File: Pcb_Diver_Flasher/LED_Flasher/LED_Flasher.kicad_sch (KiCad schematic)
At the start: 24 parts, among them IC100 PIC16LF15313, IC101 MP3217, J100 SKEDD6, SW100 MK15-C2, T100 MJD122T4

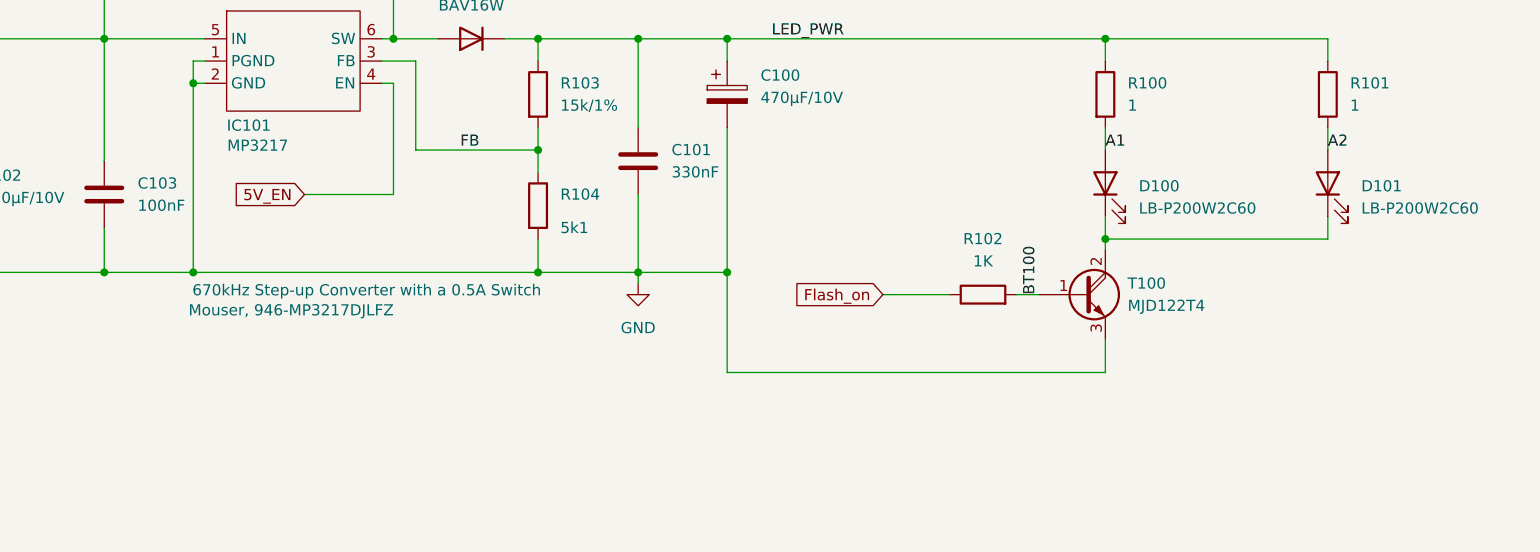
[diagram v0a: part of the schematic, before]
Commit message: New datasheets and simulations added. Target is to improve the power of the booster circuit of the diver flasher.
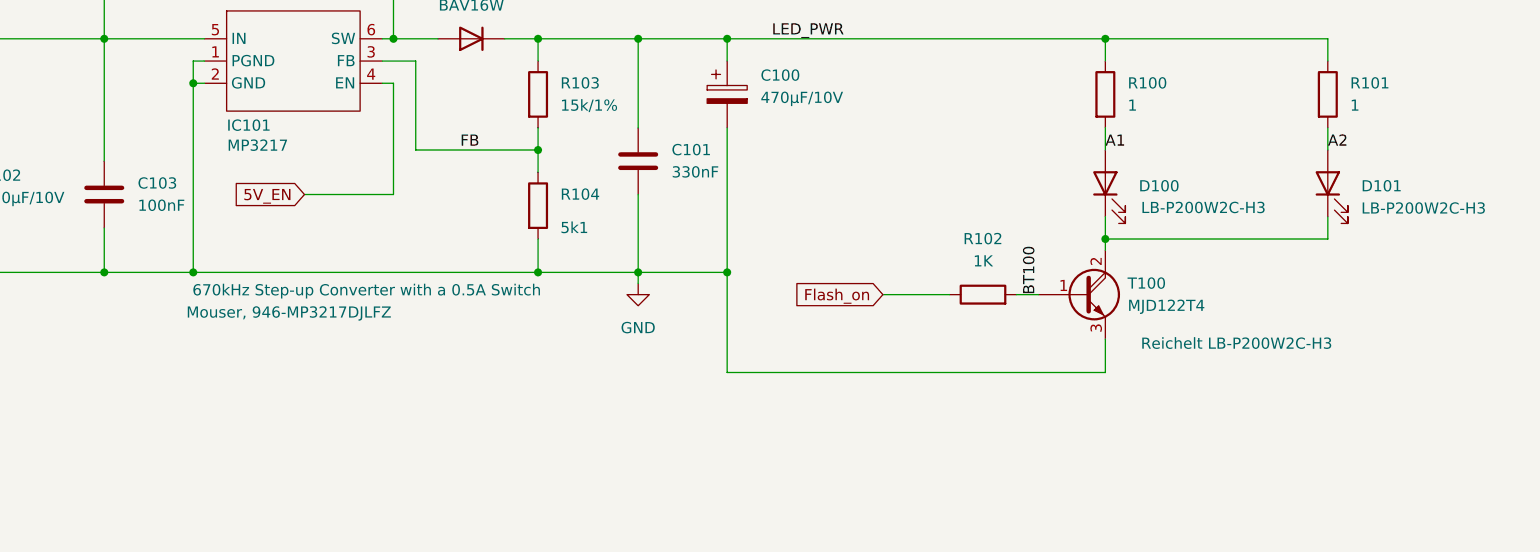
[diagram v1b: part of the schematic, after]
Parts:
- D100: value LB-P200W2C60 -> LB-P200W2C-H3; Supplier1 (none) -> Reichelt LB-P200W2C-H3
- D101: value LB-P200W2C60 -> LB-P200W2C-H3
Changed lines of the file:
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@@
 			)
 		)
-		(property "Value" "LB-P200W2C60"
+		(property "Value" "LB-P200W2C-H3"
 			(at 237.49 52.3874 90)
 			(effects
@@
 		(on_board yes)
 		(dnp no)
-		(fields_autoplaced yes)
 		(property "Reference" "D100"
 			(at 212.09 49.8474 90)
@@
 			)
 		)
-		(property "Value" "LB-P200W2C60"
-			(at 212.09 52.3874 90)
+		(property "Value" "LB-P200W2C-H3"
+			(at 212.344 52.324 90)
 			(effects
 				(font
@@
 			)
 		)
+		(property "Supplier1" "Reichelt LB-P200W2C-H3"
+			(at 223.266 67.818 90)
+			(effects
+				(font
+					(size 1.27 1.27)
+				)
+			)
+		)
 		(pin "1"
 		)
@@
 		)
 		(property "Supplier1" "Mouser, 946-MP3217DJLFZ "
-			(at 115.316 64.008 0)
-			(effects
-				(font
+			(at 115.062 64.262 0)
+			(effects
+				(font

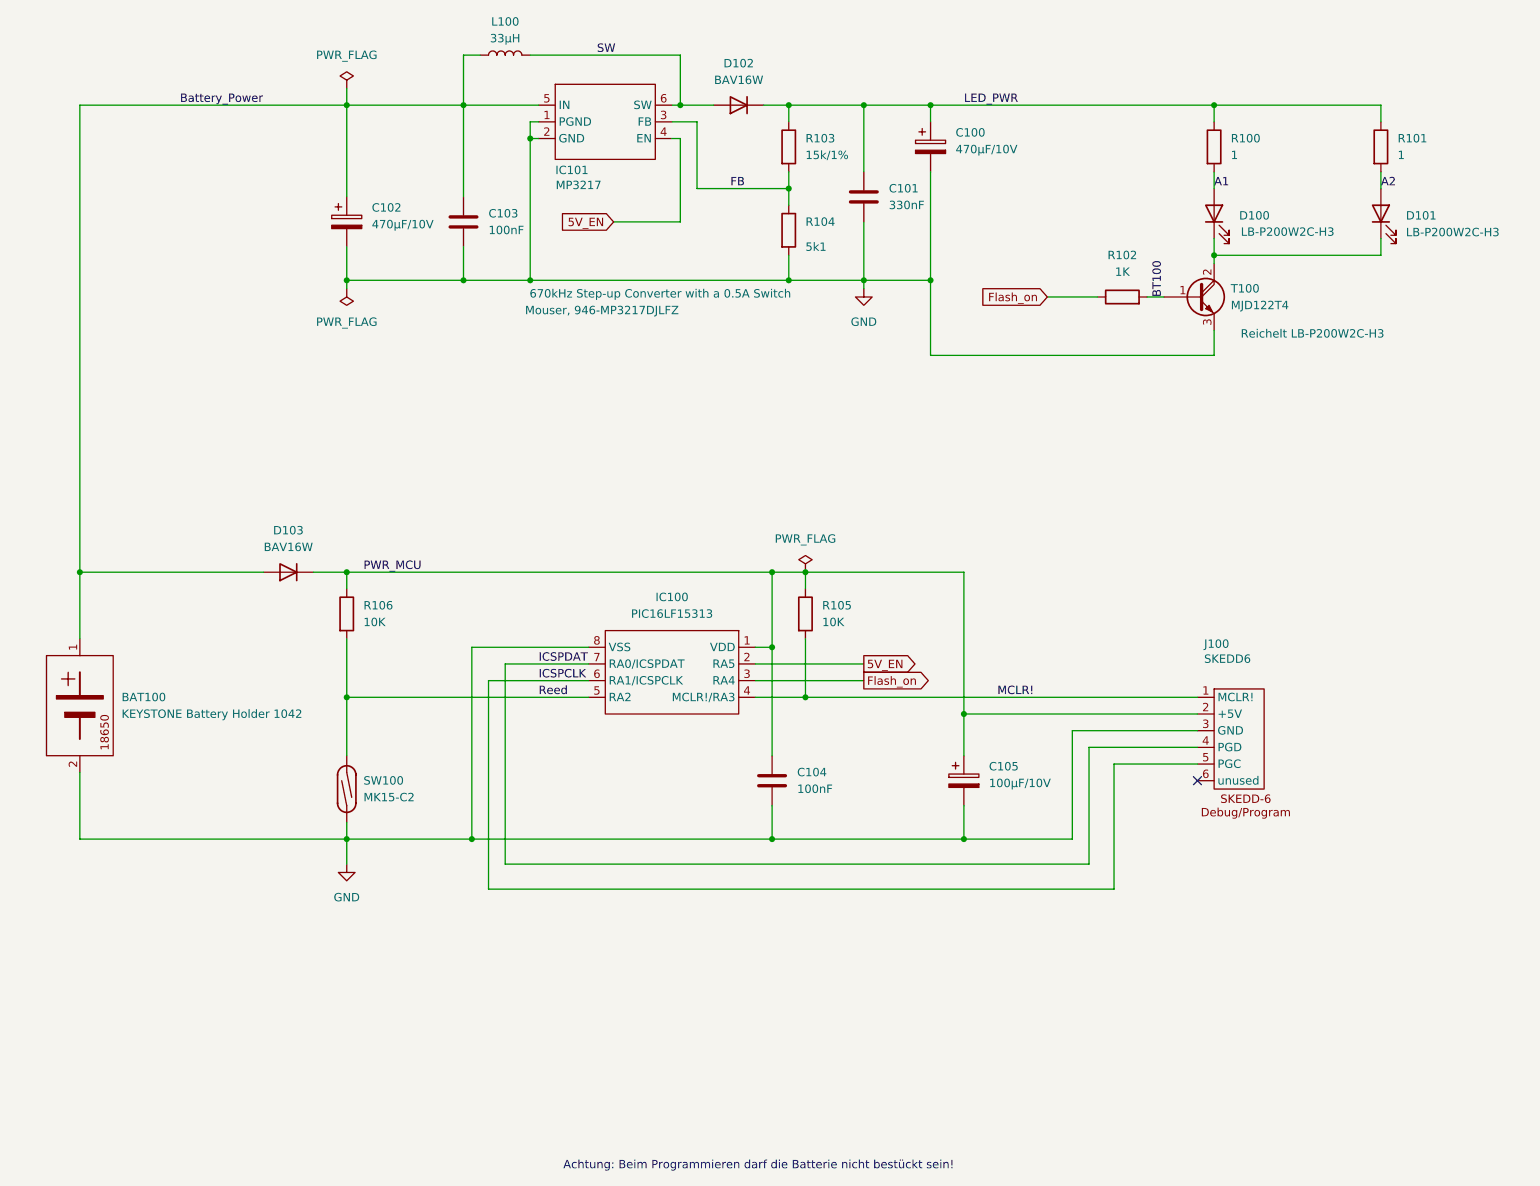
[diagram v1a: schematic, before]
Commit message: Started with version 1.1 of the dive flasher PCB. 1.0 => old too weak booster 1.1 => new hopefully more powerful booster
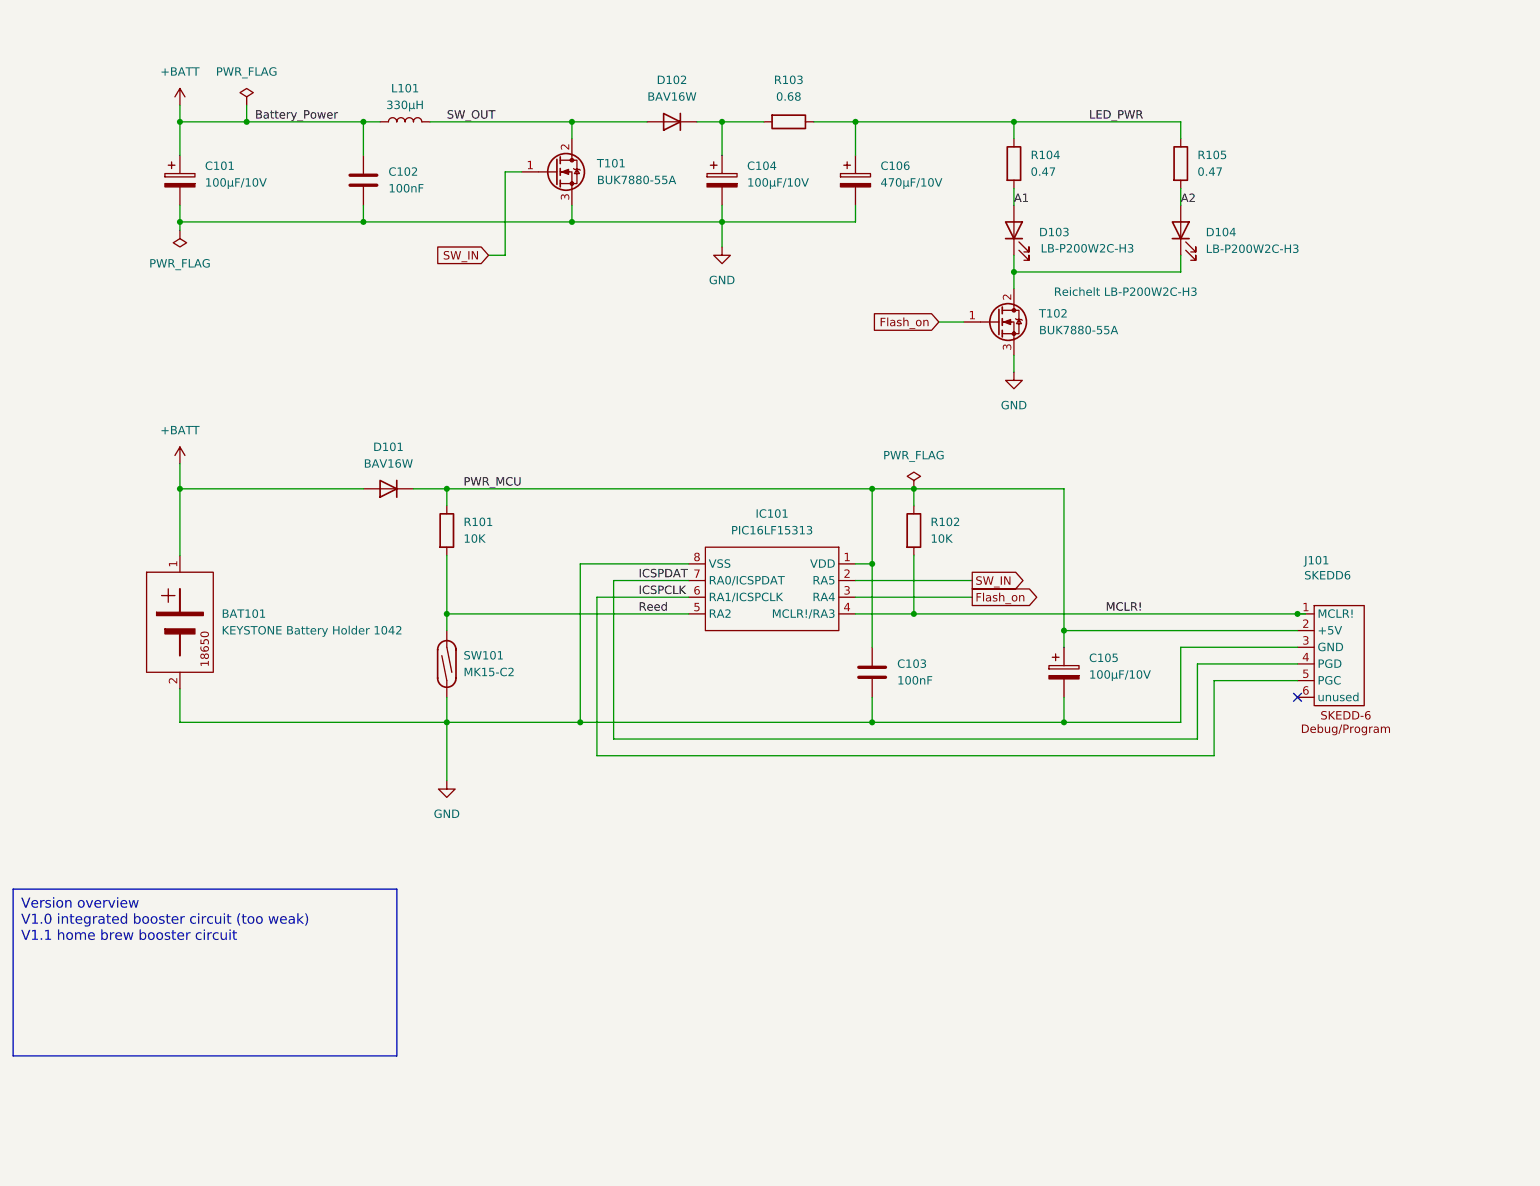
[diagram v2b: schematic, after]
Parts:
- removed C101: 330nF, Capacitor_SMD:C_0805_2012Metric_Pad1.18x1.45mm_HandSolder, symbol Device:C
- removed C102: 470µF/10V, Capacitor_SMD:CP_Elec_6.3x7.7, symbol Device:C_Polarized
- removed IC101: MP3217, Package_TO_SOT_SMD:TSOT-23-6, symbol MyPower:MP3217_1
- removed R103: 15k/1%, Resistor_SMD:R_0805_2012Metric_Pad1.20x1.40mm_HandSolder, symbol Device:R
- removed R104: 5k1, Resistor_SMD:R_0805_2012Metric_Pad1.20x1.40mm_HandSolder, symbol Device:R
- removed T100: MJD122T4, Package_TO_SOT_SMD:TO-263-2, symbol Device:Q_NPN_Darlington_BCE
- added C101, C104: 100µF/10V, Capacitor_SMD:CP_Elec_6.3x7.7, symbol Device:C_Polarized
- added T101, T102: BUK7880-55A, Package_TO_SOT_SMD:SOT-223-3_TabPin2, symbol Transistor_FET:BUK7880-55A
- L101: renamed from L100; value 33µH -> 330µH
- R103: renamed from R102; value 1K -> 0.68
- R104: renamed from R100; value 1 -> 0.47
- R105: renamed from R101; value 1 -> 0.47
- renumbered BAT100 to BAT101, C103 to C102, C104 to C103, C100 to C106, D103 to D101, D100 to D103, D101 to D104, IC100 to IC101, J100 to J101, R106 to R101, R105 to R102, SW100 to SW101
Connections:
- net Flash_on: now also T102.1 (G); no longer R103.1
- net GND: now also C101.2, C104.2, T101.3 (S), T102.3 (S)
- net LED_PWR: now also R103.1; no longer D102.1 (K)
- net at D103.1 (K), D104.1 (K): now also T102.2 (D)
- net 5V_EN renamed SW_IN
- net SW_IN: now also T101.1 (G)
- net BT100: no longer names the net of R103.2
- net BT100: now also D102.1 (K), C104.1
- net Battery_Power renamed +BATT
- net +BATT: now also C101.1
- net SW renamed SW_OUT
- net SW_OUT: now also T101.2 (D)
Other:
- note removed: "Achtung: Beim Programmieren darf die Batterie nicht bestückt sein!"
- moved on the sheet: BAT101, C102, C103, C105, C106, D101, D102, D103, D104, IC101, J101, L101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
